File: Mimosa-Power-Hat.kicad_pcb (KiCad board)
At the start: 2 copper layers, 65 x 56 mm, 76 parts, among them J1 Screw_Terminal_01x04, J2 Screw_Terminal_01x02, J3 40HAT, J4 Screw_Terminal_01x02, J5 Screw_Terminal_01x04, J9 CONN_01X02, M1 Fan_Tacho_PWM, Q1 DMG2305UX, Q2 DMMT5401, U1 ADM3490ExR, U2 CAT24C32, U3 TCAN330, U4 LMZ13608, U5 AB0805, U6 MCP2515-xSO, U7 TXB0102DCU, Y1 32.768 kHz, Y2 8MHz

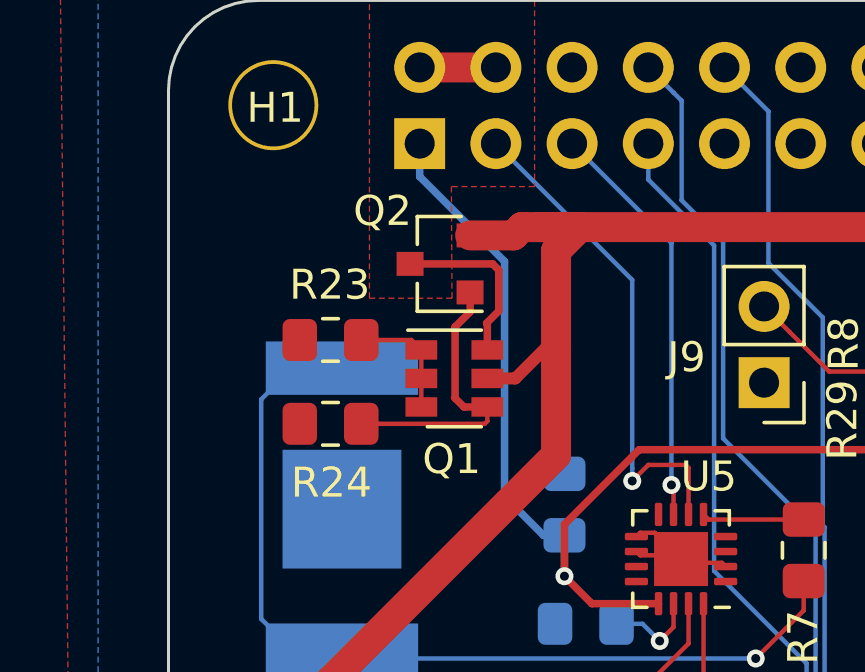
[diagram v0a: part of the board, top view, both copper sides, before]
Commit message: Correction of silk postion of Q1 and Q2
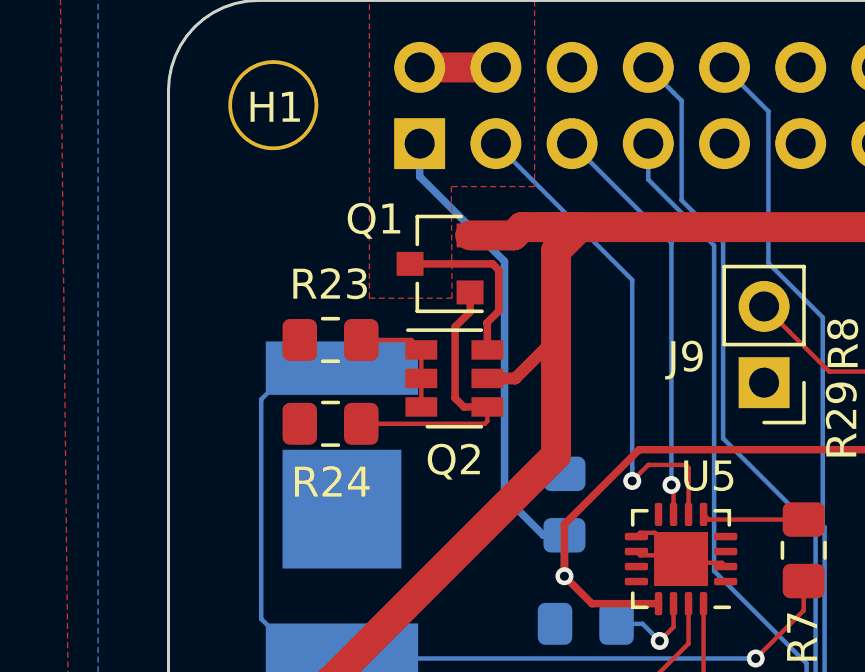
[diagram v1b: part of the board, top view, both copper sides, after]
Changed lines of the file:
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@@
   (page A4)
   (layers
-    (0 F.Cu signal hide)
+    (0 F.Cu signal)
     (31 B.Cu signal hide)
     (32 B.Adhes user hide)
@@
     (35 F.Paste user hide)
     (36 B.SilkS user hide)
-    (37 F.SilkS user hide)
+    (37 F.SilkS user)
     (38 B.Mask user hide)
     (39 F.Mask user hide)
@@
     (tags SOT-23)
     (attr smd)
-    (fp_text reference Q1 (at -0.3856 -6.50856 180) (layer F.SilkS)
+    (fp_text reference Q1 (at 2.1798 1.4772 180) (layer F.SilkS)
       (effects (font (size 1 1) (thickness 0.15)))
     )
@@
     (tags SOT-23-6)
     (attr smd)
-    (fp_text reference Q2 (at -2.39268 -5.58038) (layer F.SilkS)
+    (fp_text reference Q2 (at 0.0127 2.7305) (layer F.SilkS)
       (effects (font (size 1 1) (thickness 0.15)))
     )

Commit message: update to Kicad 6
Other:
- net class Default removed
- net class Power removed
